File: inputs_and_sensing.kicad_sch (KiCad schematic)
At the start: 2 parts, among them U8 TLP293(GB-TPL,E

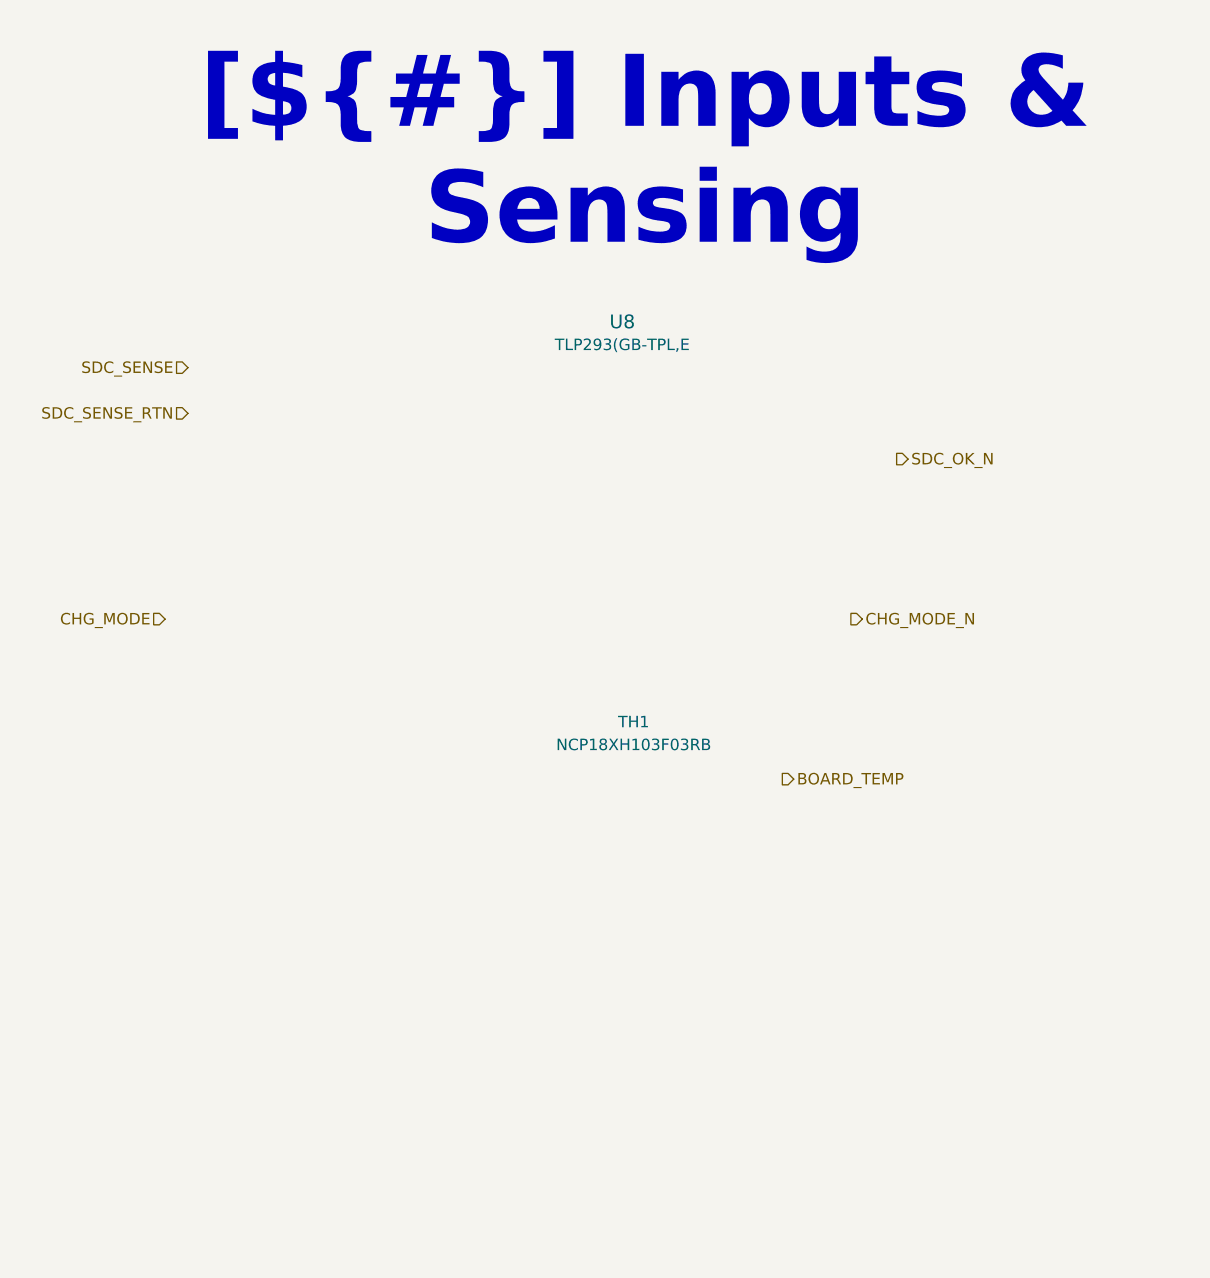
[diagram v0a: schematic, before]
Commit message: SCH[Logic, Connectors]: Removed watchdog timer going to use just stm32 interal watchdog, and com master faults. This is to simplfiy hardware less parts not needed. Adding DNP conector for halleffect sensor.
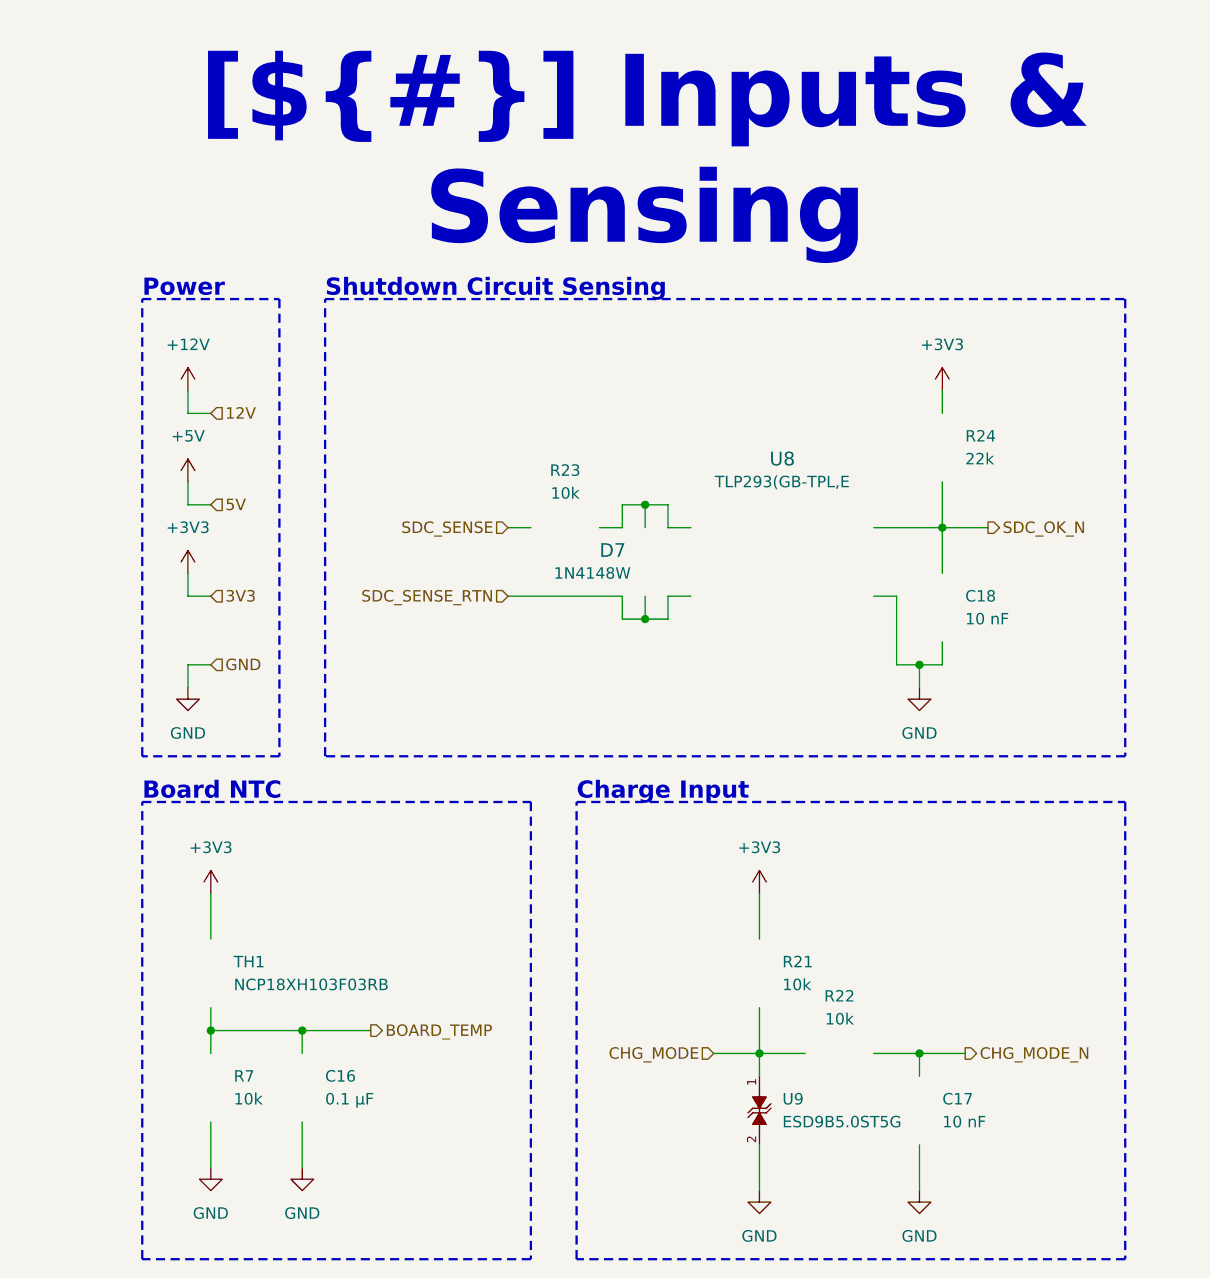
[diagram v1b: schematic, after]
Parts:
- added C16: 0.1 µF, remote_cl05a105ko5nnnc:C_0402_1005Metric, symbol remote_gcm155r71h104ke02j:C
- added C17, C18: 10 nF, remote_cl05a105ko5nnnc:C_0402_1005Metric, symbol remote_c0402c103k5recauto:C
- added D7: 1N4148W, remote_1n4148w:P35_SOD-123F, symbol remote_1n4148w:1N4148W
- added R21, R22, R7: 10k, remote_rcs060359r0fkea:R_0603_1608Metric, symbol remote_rc0402jr-0710kl:RT0402BRD0710KL
- added R23: 10k, remote_crcw080510k0fkea:R_0805_2012Metric, symbol remote_crcw080510k0fkea:R_US
- added R24: 22k, remote_rcs060359r0fkea:R_0603_1608Metric, symbol remote_crcw060322k0fkea:R_US
- added U9: ESD9B5.0ST5G, remote_esd9b3.3st5g:SODFL1006X40N, symbol remote_esd9b5.0st5g:ESD9B5.0ST5G
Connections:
- net BOARD_TEMP: now also TH1.2, C16.2, R7.2
- net CHG_MODE: now also R21.1, R22.1, U9.1
- net CHG_MODE_N: now also C17.1, R22.2
- net SDC_OK_N: now also U8.4, C18.1, R24.1
- net SDC_SENSE: now also R23.1
- net SDC_SENSE_RTN: now also U8.2, D7.2 (A)
- net at U8.1: now also D7.1 (K), R23.2
- net GND: now reaches U8.3
- net GND: now also C16.1, C17.2, C18.2, R7.1, U9.2
- net +3V3: now reaches TH1.1
- net +3V3: now also R21.2, R24.2
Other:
- note added: "Board NTC"
- note added: "Charge Input"
- note added: "Power"
- note added: "Shutdown Circuit Sensing"

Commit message: PCB[Layout, Mounting]:Inital layout and edgecut/hole placment.
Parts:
- renumbered C18 to C13, C17 to C14, C16 to C15, R24 to R22, R21 to R24, R22 to R25, R7 to R26, U8 to U7, U9 to U8
